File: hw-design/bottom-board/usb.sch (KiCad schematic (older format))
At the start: 14 parts, among them P1 USB_B, P2 USB_A, U10 RT9701

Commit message: Changed SODIM to Marsboard header + added liniar regulator for audio codec
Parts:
- U10: symbol Power_Management:RT9701 -> bottom-board-rescue:RT9701-Power_Management
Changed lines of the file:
@@
 $EndComp
 $Comp
-L power:GNDD #PWR0125
+L bottom-board-rescue:GNDD-power #PWR0175
 U 1 1 5509E7DC
 P 3450 3150
-F 0 "#PWR0125" H 3450 2900 50  0001 C CNN
+F 0 "#PWR0175" H 3450 2900 50  0001 C CNN
 F 1 "GNDD" H 3450 3000 50  0000 C CNN
 F 2 "" H 3450 3150 60  0000 C CNN
@@
 $EndComp
 $Comp
-L power:GNDD #PWR0126
+L bottom-board-rescue:GNDD-power #PWR0176
 U 1 1 5509F619
 P 2550 3850
-F 0 "#PWR0126" H 2550 3600 50  0001 C CNN
+F 0 "#PWR0176" H 2550 3600 50  0001 C CNN
 F 1 "GNDD" H 2550 3700 50  0000 C CNN
 F 2 "" H 2550 3850 60  0000 C CNN
@@
 $EndComp
 $Comp
-L power:GNDD #PWR0127
+L bottom-board-rescue:GNDD-power #PWR0177
 U 1 1 550A00BD
 P 4750 3850
-F 0 "#PWR0127" H 4750 3600 50  0001 C CNN
+F 0 "#PWR0177" H 4750 3600 50  0001 C CNN
 F 1 "GNDD" H 4750 3700 50  0000 C CNN
 F 2 "" H 4750 3850 60  0000 C CNN
@@
 $EndComp
 $Comp
-L power:GNDD #PWR0128
+L bottom-board-rescue:GNDD-power #PWR0178
 U 1 1 550A60A5
 P 9050 3200
-F 0 "#PWR0128" H 9050 2950 50  0001 C CNN
+F 0 "#PWR0178" H 9050 2950 50  0001 C CNN
 F 1 "GNDD" H 9050 3050 50  0000 C CNN
 F 2 "" H 9050 3200 60  0000 C CNN
@@
 $EndComp
 $Comp
-L power:GNDD #PWR0129
+L bottom-board-rescue:GNDD-power #PWR0179
 U 1 1 550A73CA
 P 9350 2750
-F 0 "#PWR0129" H 9350 2500 50  0001 C CNN
+F 0 "#PWR0179" H 9350 2500 50  0001 C CNN
 F 1 "GNDD" H 9350 2600 50  0000 C CNN
 F 2 "" H 9350 2750 60  0000 C CNN
@@
 $EndComp
 $Comp
-L Power_Management:RT9701 U10
+L bottom-board-rescue:RT9701-Power_Management U10
 U 1 1 55080DFB
 P 7850 3550
@@
 $EndComp
 $Comp
-L power:GNDD #PWR0130
+L bottom-board-rescue:GNDD-power #PWR0180
 U 1 1 55084544
 P 7850 4000
-F 0 "#PWR0130" H 7850 3750 50  0001 C CNN
+F 0 "#PWR0180" H 7850 3750 50  0001 C CNN
 F 1 "GNDD" H 7850 3850 50  0000 C CNN
 F 2 "" H 7850 4000 60  0000 C CNN
@@
 $EndComp
 $Comp
-L power:+5V #PWR0131
+L bottom-board-rescue:+5V-power #PWR0181
 U 1 1 55085DDA
 P 7250 3000
-F 0 "#PWR0131" H 7250 2850 50  0001 C CNN
+F 0 "#PWR0181" H 7250 2850 50  0001 C CNN
 F 1 "+5V" H 7250 3140 50  0000 C CNN
 F 2 "" H 7250 3000 60  0000 C CNN
@@
 $EndComp
 $Comp
-L power:GNDD #PWR0132
+L bottom-board-rescue:GNDD-power #PWR0182
 U 1 1 5508613A
 P 7750 3150
-F 0 "#PWR0132" H 7750 2900 50  0001 C CNN
+F 0 "#PWR0182" H 7750 2900 50  0001 C CNN
 F 1 "GNDD" H 7750 3000 50  0000 C CNN
 F 2 "" H 7750 3150 60  0000 C CNN
@@
 $EndComp
 $Comp
-L power:GNDD #PWR0133
+L bottom-board-rescue:GNDD-power #PWR0183
 U 1 1 551E6B87
 P 10400 3900
-F 0 "#PWR0133" H 10400 3650 50  0001 C CNN
+F 0 "#PWR0183" H 10400 3650 50  0001 C CNN
 F 1 "GNDD" H 10400 3750 50  0000 C CNN
 F 2 "" H 10400 3900 60  0000 C CNN

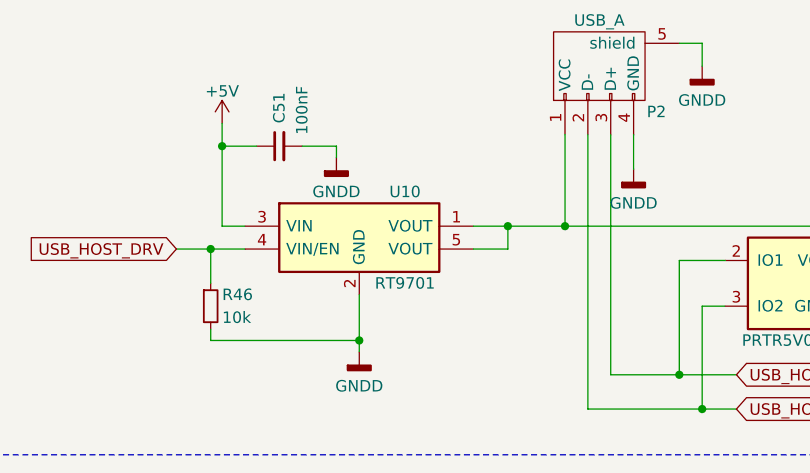
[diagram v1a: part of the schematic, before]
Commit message: Changed U10 to another chip due to unavailability
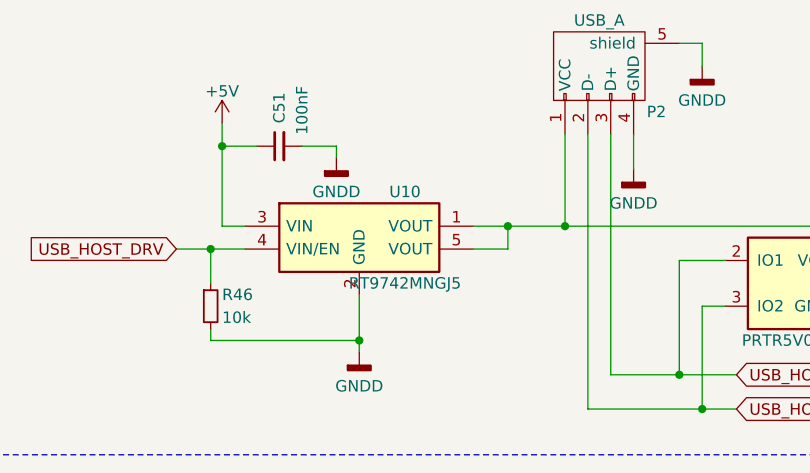
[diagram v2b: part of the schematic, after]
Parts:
- U10: value RT9701 -> RT9742MNGJ5; MPN RT9701GB -> RT9742MNGJ5
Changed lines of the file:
@@
 P 7850 3550
 F 0 "U10" H 8050 3800 50  0000 C CNN
-F 1 "RT9701" H 8050 3400 50  0000 C CNN
+F 1 "RT9742MNGJ5" H 8050 3400 50  0000 C CNN
 F 2 "Housings_SOT-23_SOT-143_TSOT-6:SOT-23-5" H 7850 3550 60  0001 C CNN
-F 3 "" H 7850 3550 60  0000 C CNN
-F 4 "RT9701GB" H 250 0   50  0001 C CNN "MPN"
+F 3 "https://www.richtek.com/assets/product_file/RT9742/DS9742-07.pdf" H 6950 4600 60  0001 C CNN
+F 4 "RT9742MNGJ5" H 250 0   50  0001 C CNN "MPN"
 	1    7850 3550
 	1    0    0    -1
@@
 Text GLabel 9500 4250 2    50   BiDi ~ 0
 USB_HOST_DM
-Text GLabel 7050 3550 0    50   Input ~ 0
-USB_HOST_DRV
 Text Notes 1050 2350 0    100  ~ 0
 USB DEVICE
@@
 Wire Wire Line
 	3150 3200 3150 3400
+Text GLabel 7050 3550 0    50   Input ~ 0
+USB_HOST_DRV
 $EndSCHEMATC

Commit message: updated footprints and MPN's
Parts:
- C48, C50, C51, C52: footprint Capacitors_SMD:C_0603 -> Capacitor_SMD:C_0603_1608Metric
- C49, L1: footprint Capacitors_SMD:C_0805 -> Capacitor_SMD:C_0805_2012Metric
- D13, D14: footprint Housings_SOT-23_SOT-143_TSOT-6:SOT-143 -> Package_TO_SOT_SMD:SOT-143
- P1: footprint Connect:USB_B -> Connector_USB:USB_B_OST_USB-B1HSxx_Horizontal
- R42, R43, R46: footprint Resistors_SMD:R_0603 -> Resistor_SMD:R_0603_1608Metric
- U10: footprint Housings_SOT-23_SOT-143_TSOT-6:SOT-23-5 -> Package_TO_SOT_SMD:SOT-23-5
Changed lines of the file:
@@
 EESchema Schematic File Version 4
 LIBS:bottom-board-cache
-EELAYER 26 0
+EELAYER 29 0
 EELAYER END
 $Descr A4 11693 8268
@@
 F 0 "D13" H 3700 3650 50  0000 C CNN
 F 1 "PRTR5V0U2X" H 4000 3400 50  0000 C CNN
-F 2 "Housings_SOT-23_SOT-143_TSOT-6:SOT-143" H 4050 3600 60  0001 C CNN
+F 2 "Package_TO_SOT_SMD:SOT-143" H 4050 3600 60  0001 C CNN
 F 3 "" H 4050 3600 60  0000 C CNN
 F 4 "PRTR5V0U2X,215" H -200 -50 50  0001 C CNN "MPN"
@@
 F 0 "L1" H 3800 2950 50  0000 L CNN
 F 1 "600R 1.5A" H 3800 2850 50  0000 L CNN
-F 2 "Capacitors_SMD:C_0805" H 3750 2900 60  0001 C CNN
+F 2 "Capacitor_SMD:C_0805_2012Metric" H 3750 2900 60  0001 C CNN
 F 3 "" H 3750 2900 60  0000 C CNN
 F 4 "MI0805K601R-10" H -100 -50 50  0001 C CNN "MPN"
@@
 F 0 "R42" H 2600 3400 50  0000 L CNN
 F 1 "5k6" H 2600 3300 50  0000 L CNN
-F 2 "Resistors_SMD:R_0603" H 2550 3350 60  0001 C CNN
+F 2 "Resistor_SMD:R_0603_1608Metric" H 2550 3350 60  0001 C CNN
 F 3 "" H 2550 3350 60  0000 C CNN
 F 4 "RMCF0603JT5K60" H 350 -50 50  0001 C CNN "MPN"
@@
 F 0 "R43" H 2600 3700 50  0000 L CNN
 F 1 "10k" H 2600 3600 50  0000 L CNN
-F 2 "Resistors_SMD:R_0603" H 2550 3650 60  0001 C CNN
+F 2 "Resistor_SMD:R_0603_1608Metric" H 2550 3650 60  0001 C CNN
 F 3 "" H 2550 3650 60  0000 C CNN
 F 4 "RMCF0603JT10K0" H 350 -50 50  0001 C CNN "MPN"
@@
 F 0 "C48" H 2100 3650 50  0000 L CNN
 F 1 "100nF" H 2050 3550 50  0000 L CNN
-F 2 "Capacitors_SMD:C_0603" H 2300 3650 60  0001 C CNN
+F 2 "Capacitor_SMD:C_0603_1608Metric" H 2300 3650 60  0001 C CNN
 F 3 "" H 2300 3650 60  0000 C CNN
 F 4 "C1608X7R1E104K080AA" H 350 -50 50  0001 C CNN "MPN"
@@
 F 0 "C50" H 4760 3670 50  0000 L CNN
 F 1 "100nF" H 4760 3520 50  0000 L CNN
-F 2 "Capacitors_SMD:C_0603" H 4750 3600 60  0001 C CNN
+F 2 "Capacitor_SMD:C_0603_1608Metric" H 4750 3600 60  0001 C CNN
 F 3 "" H 4750 3600 60  0000 C CNN
 F 4 "C1608X7R1E104K080AA" H -100 -50 50  0001 C CNN "MPN"
@@
 F 0 "U10" H 8050 3800 50  0000 C CNN
 F 1 "RT9742MNGJ5" H 8050 3400 50  0000 C CNN
-F 2 "Housings_SOT-23_SOT-143_TSOT-6:SOT-23-5" H 7850 3550 60  0001 C CNN
+F 2 "Package_TO_SOT_SMD:SOT-23-5" H 7850 3550 60  0001 C CNN
 F 3 "https://www.richtek.com/assets/product_file/RT9742/DS9742-07.pdf" H 6950 4600 60  0001 C CNN
 F 4 "RT9742MNGJ5" H 250 0   50  0001 C CNN "MPN"
@@
 F 0 "R46" H 7250 3850 50  0000 L CNN
 F 1 "10k" H 7250 3750 50  0000 L CNN
-F 2 "Resistors_SMD:R_0603" H 7200 3800 60  0001 C CNN
+F 2 "Resistor_SMD:R_0603_1608Metric" H 7200 3800 60  0001 C CNN
 F 3 "" H 7200 3800 60  0000 C CNN
 F 4 "RMCF0603JT10K0" H 250 0   50  0001 C CNN "MPN"
@@
 F 0 "C51" H 7600 3100 50  0000 L CNN
 F 1 "100nF" H 7550 3000 50  0000 L CNN
-F 2 "Capacitors_SMD:C_0603" H 7500 3100 60  0001 C CNN
+F 2 "Capacitor_SMD:C_0603_1608Metric" H 7500 3100 60  0001 C CNN
 F 3 "" H 7500 3100 60  0000 C CNN
 F 4 "C1608X7R1E104K080AA" H 250 0   50  0001 C CNN "MPN"
@@
 F 0 "D14" H 9450 3700 50  0000 C CNN
 F 1 "PRTR5V0U2X" H 9750 3450 50  0000 C CNN
-F 2 "Housings_SOT-23_SOT-143_TSOT-6:SOT-143" H 9800 3650 60  0001 C CNN
+F 2 "Package_TO_SOT_SMD:SOT-143" H 9800 3650 60  0001 C CNN
 F 3 "" H 9800 3650 60  0000 C CNN
 F 4 "PRTR5V0U2X,215" H 250 0   50  0001 C CNN "MPN"
@@
 F 0 "C52" H 10410 3720 50  0000 L CNN
 F 1 "100nF" H 10410 3570 50  0000 L CNN
-F 2 "Capacitors_SMD:C_0603" H 10400 3650 60  0001 C CNN
+F 2 "Capacitor_SMD:C_0603_1608Metric" H 10400 3650 60  0001 C CNN
 F 3 "" H 10400 3650 60  0000 C CNN
 F 4 "C1608X7R1E104K080AA" H 250 0   50  0001 C CNN "MPN"
@@
 F 0 "C49" H 2900 3550 50  0000 L CNN
 F 1 "10uF" H 2900 3450 50  0000 L CNN
-F 2 "Capacitors_SMD:C_0805" H 2800 3500 60  0001 C CNN
+F 2 "Capacitor_SMD:C_0805_2012Metric" H 2800 3500 60  0001 C CNN
 F 3 "" H 2800 3500 60  0000 C CNN
 F 4 "GRM219R61E106KA12D" H -2500 -1850 50  0001 C CNN "MPN"
@@
 F 0 "P1" H 3550 2500 50  0000 C CNN
 F 1 "USB_B" H 3300 2900 50  0000 C CNN
-F 2 "Connect:USB_B" V 3300 2600 60  0001 C CNN
+F 2 "Connector_USB:USB_B_OST_USB-B1HSxx_Horizontal" V 3300 2600 60  0001 C CNN
 F 3 "" V 3300 2600 60  0000 C CNN
 F 4 "61729-1011BLF" H 3350 2700 60  0001 C CNN "MPN"
